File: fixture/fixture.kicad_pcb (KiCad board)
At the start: 2 copper layers, 100 x 100 mm, 40 parts, among them J1 Conn_Coaxial, J10 Conn_Coaxial, J11 Conn_Coaxial, J12 Conn_Coaxial, J13 Conn_Coaxial, J14 Conn_Coaxial, J15 Conn_Coaxial, J16 Conn_Coaxial, J17 Conn_Coaxial, J18 Conn_01x01, J19 Conn_01x01, J2 Conn_Coaxial, J20 Conn_01x01, J21 Conn_01x01, J22 Conn_Coaxial, J23 Conn_Coaxial, J24 Conn_Coaxial, J25 Conn_Coaxial, J26 Conn_01x02, J27 Conn_Coaxial, J28 Conn_01x02, J29 Conn_Coaxial, J3 Conn_Coaxial, J30 Conn_01x01, J31 Conn_01x01, J32 Conn_Coaxial, J4 Conn_02x08_Counter_Clockwise, J5 Conn_02x08_Counter_Clockwise, J6 Conn_Coaxial, J7 Conn_Coaxial, J8 Conn_Coaxial, J9 Conn_Coaxial

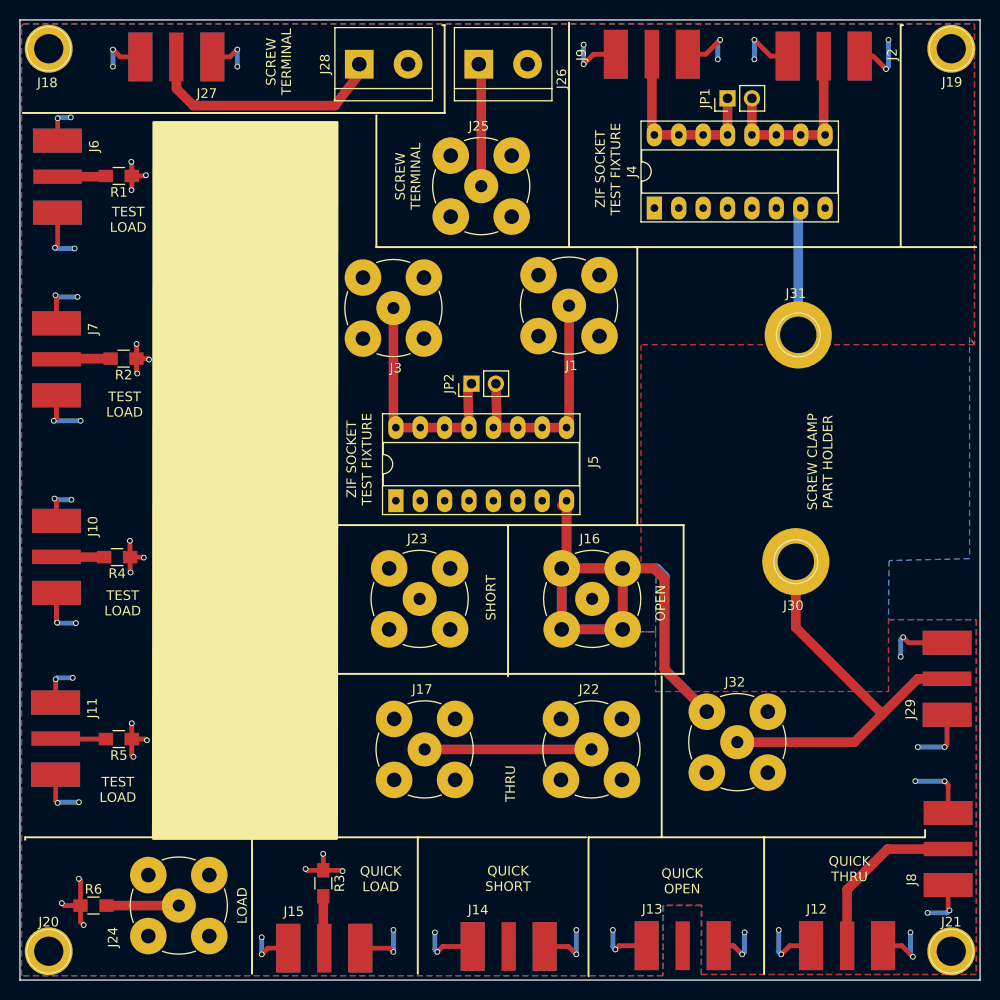
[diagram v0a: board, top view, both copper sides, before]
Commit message: Made more room for handle of ZIF socket
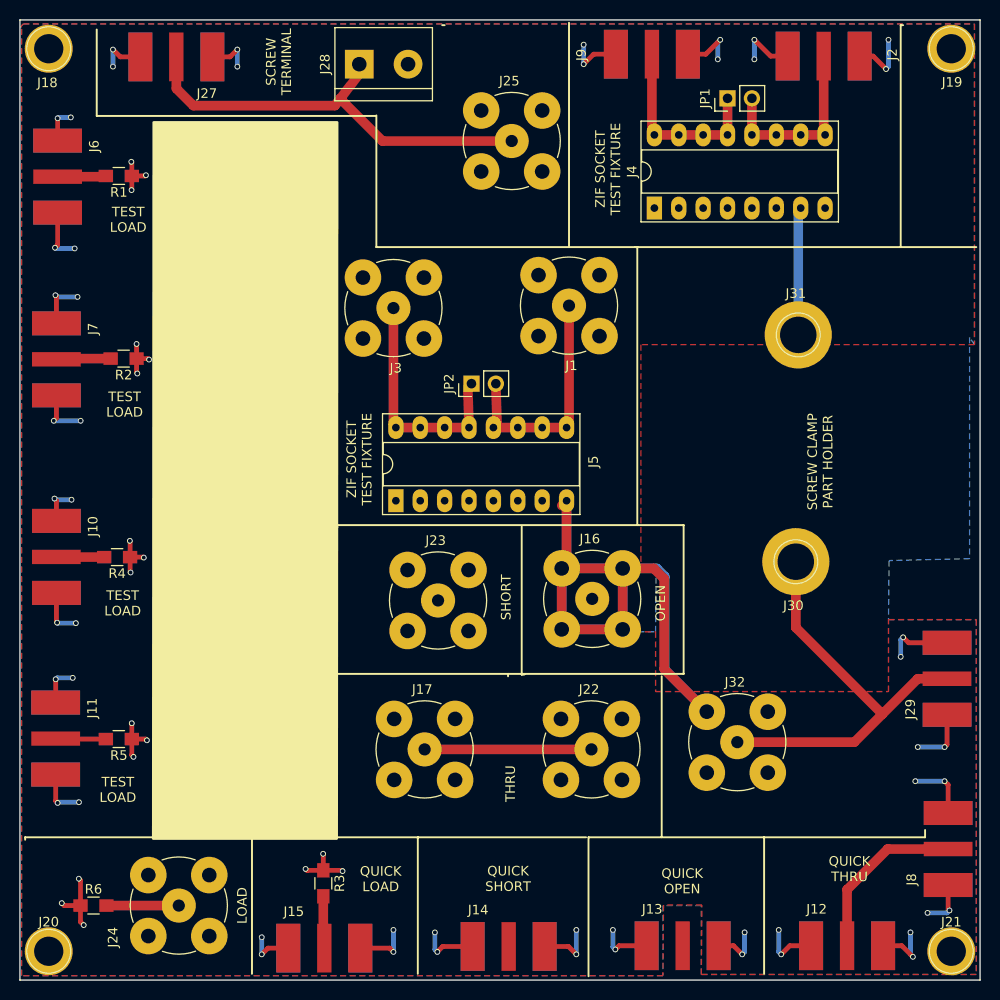
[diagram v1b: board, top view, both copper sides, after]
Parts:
- removed J26: Conn_01x02, Connectors_Terminal_Blocks:TerminalBlock_bornier-2_P5.08mm
- moved J25 5.67 mm to (101.2, 62.6)
- moved J23 1.92 mm to (93.5, 110.5)
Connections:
- J27 pad 1: Net-(J27-Pad1) -> Net-(J25-Pad1)
- J28 pad 1: Net-(J27-Pad1) -> Net-(J25-Pad1)
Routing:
- net Net-(J25-Pad1): track 12.8 -> 45.4 mm
- net Net-(J27-Pad1): track 25.7 -> 0.00 mm
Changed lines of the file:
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@@
 (kicad_pcb (version 4) (host pcbnew 4.0.7)
   (general
-    (links 150)
+    (links 149)
     (no_connects 0)
     (area 49.924999 49.924999 150.075001 150.075001)
     (thickness 1.6)
     (drawings 53)
-    (tracks 283)
+    (tracks 284)
     (zones 0)
-    (modules 40)
-    (nets 17)
+    (modules 39)
+    (nets 16)
   )
   (page A4)
@@
   (net 13 "Net-(J24-Pad1)")
   (net 14 "Net-(J25-Pad1)")
-  (net 15 "Net-(J27-Pad1)")
-  (net 16 "Net-(J29-Pad1)")
+  (net 15 "Net-(J29-Pad1)")
   (net_class Default "This is the default net class."
     (clearance 0.2)
@@
     (add_net "Net-(J24-Pad1)")
     (add_net "Net-(J25-Pad1)")
-    (add_net "Net-(J27-Pad1)")
     (add_net "Net-(J29-Pad1)")
     (add_net "Net-(J3-Pad1)")
@@
   )
   (module Connectors:bnc-ci (layer F.Cu)
-    (at 91.6305 110.2995)
+    (at 93.5482 110.4646)
     (descr "BNC female PCB mount 4 pin straight chassis connector")
     (tags "BNC female PCB mount 4 pin straight chassis connector http://img-asia.electrocomponents.com/largeimages/L457024-02.gif")
@@
   )
   (module Connectors:bnc-ci (layer F.Cu)
-    (at 98.044 67.31)
+    (at 101.219 62.611)
     (descr "BNC female PCB mount 4 pin straight chassis connector")
     (tags "BNC female PCB mount 4 pin straight chassis connector http://img-asia.electrocomponents.com/largeimages/L457024-02.gif")
@@
       (at (xyz 0 0 0))
       (scale (xyz 2 2 2))
-      (rotate (xyz 0 0 0))
-    )
-  )
-  (module Connectors_Terminal_Blocks:TerminalBlock_bornier-2_P5.08mm (layer F.Cu)
-    (at 97.79 54.61)
-    (descr "simple 2-pin terminal block, pitch 5.08mm, revamped version of bornier2")
-    (tags "terminal block bornier2")
-    (fp_text reference J26 (at 8.636 1.524 270) (layer F.SilkS)
-      (effects (font (size 1 1) (thickness 0.15)))
-    )
-    (fp_text value Conn_01x02 (at 2.54 5.08) (layer F.Fab)
-      (effects (font (size 1 1) (thickness 0.15)))
-    )
-    (fp_text user %R (at 2.54 0) (layer F.Fab)
-      (effects (font (size 1 1) (thickness 0.15)))
-    )
-    (fp_line (start -2.41 2.55) (end 7.49 2.55) (layer F.Fab) (width 0.1))
-    (fp_line (start -2.46 -3.75) (end -2.46 3.75) (layer F.Fab) (width 0.1))
-    (fp_line (start -2.46 3.75) (end 7.54 3.75) (layer F.Fab) (width 0.1))
-    (fp_line (start 7.54 3.75) (end 7.54 -3.75) (layer F.Fab) (width 0.1))
-    (fp_line (start 7.54 -3.75) (end -2.46 -3.75) (layer F.Fab) (width 0.1))
-    (fp_line (start 7.62 2.54) (end -2.54 2.54) (layer F.SilkS) (width 0.12))
-    (fp_line (start 7.62 3.81) (end 7.62 -3.81) (layer F.SilkS) (width 0.12))
-    (fp_line (start 7.62 -3.81) (end -2.54 -3.81) (layer F.SilkS) (width 0.12))
-    (fp_line (start -2.54 -3.81) (end -2.54 3.81) (layer F.SilkS) (width 0.12))
-    (fp_line (start -2.54 3.81) (end 7.62 3.81) (layer F.SilkS) (width 0.12))
-    (fp_line (start -2.71 -4) (end 7.79 -4) (layer F.CrtYd) (width 0.05))
-    (fp_line (start -2.71 -4) (end -2.71 4) (layer F.CrtYd) (width 0.05))
-    (fp_line (start 7.79 4) (end 7.79 -4) (layer F.CrtYd) (width 0.05))
-    (fp_line (start 7.79 4) (end -2.71 4) (layer F.CrtYd) (width 0.05))
-    (pad 1 thru_hole rect (at 0 0) (size 3 3) (drill 1.52) (layers *.Cu *.Mask)
-      (net 14 "Net-(J25-Pad1)"))
-    (pad 2 thru_hole circle (at 5.08 0) (size 3 3) (drill 1.52) (layers *.Cu *.Mask)
-      (net 1 GND))
-    (model ${KISYS3DMOD}/Terminal_Blocks.3dshapes/TerminalBlock_bornier-2_P5.08mm.wrl
-      (at (xyz 0.1 0 0))
-      (scale (xyz 1 1 1))
       (rotate (xyz 0 0 0))
     )
@@
       (net 1 GND))
     (pad 1 smd rect (at 0 0 180) (size 1.5 5.08) (layers F.Cu F.Paste F.Mask)
-      (net 15 "Net-(J27-Pad1)"))
+      (net 14 "Net-(J25-Pad1)"))
     (model ${KISYS3DMOD}/Connectors_Amphenol.3dshapes/Amphenol_RF_SMA_132289.wrl
       (at (xyz 0 0 0))
@@
     (fp_line (start 7.79 4) (end -2.71 4) (layer F.CrtYd) (width 0.05))
     (pad 1 thru_hole rect (at 0 0) (size 3 3) (drill 1.52) (layers *.Cu *.Mask)
-      (net 15 "Net-(J27-Pad1)"))
+      (net 14 "Net-(J25-Pad1)"))
     (pad 2 thru_hole circle (at 5.08 0) (size 3 3) (drill 1.52) (layers *.Cu *.Mask)
       (net 1 GND))
@@
       (net 1 GND))
     (pad 1 smd rect (at 0 0 90) (size 1.5 5.08) (layers F.Cu F.Paste F.Mask)
-      (net 16 "Net-(J29-Pad1)"))
+      (net 15 "Net-(J29-Pad1)"))
     (model ${KISYS3DMOD}/Connectors_Amphenol.3dshapes/Amphenol_RF_SMA_132289.wrl
       (at (xyz 0 0 0))
@@
     (fp_circle (center 0 0) (end 0 -2.286) (layer F.SilkS) (width 0.12))
     (pad 1 thru_hole circle (at 0 0) (size 7 7) (drill 3.8) (layers *.Cu *.Mask)
-      (net 16 "Net-(J29-Pad1)"))
+      (net 15 "Net-(J29-Pad1)"))
   )
   (module Connectors:1pin (layer F.Cu)
@@
       (net 1 GND))
     (pad 1 thru_hole circle (at 0 0) (size 3.556 3.556) (drill 1.27) (layers *.Cu *.Mask)
-      (net 16 "Net-(J29-Pad1)"))
+      (net 15 "Net-(J29-Pad1)"))
     (pad 2 thru_hole circle (at 3.175 -3.175) (size 3.81 3.81) (drill 1.524) (layers *.Cu *.Mask)
       (net 1 GND))
@@
     )
   )
+  (gr_line (start 102.2604 118.1862) (end 102.5398 118.1862) (angle 90) (layer F.SilkS) (width 0.2))
+  (gr_line (start 102.2604 102.7684) (end 102.2604 118.1862) (angle 90) (layer F.SilkS) (width 0.2))
+  (gr_line (start 58 60) (end 58 51) (angle 90) (layer F.SilkS) (width 0.2))
+  (gr_line (start 87 60) (end 58 60) (angle 90) (layer F.SilkS) (width 0.2))
   (gr_line (start 141.732 73.66) (end 149.606 73.66) (angle 90) (layer F.SilkS) (width 0.2))
   (gr_line (start 141.732 50.546) (end 141.986 50.546) (angle 90) (layer F.SilkS) (width 0.2))
@@
   (gr_line (start 114.3 102.616) (end 119.126 102.616) (angle 90) (layer F.SilkS) (width 0.2))
   (gr_line (start 100.838 118.11) (end 83.058 118.11) (angle 90) (layer F.SilkS) (width 0.2))
-  (gr_line (start 100.838 102.616) (end 100.838 118.11) (angle 90) (layer F.SilkS) (width 0.2))
   (gr_line (start 83.058 102.616) (end 83.058 102.87) (angle 90) (layer F.SilkS) (width 0.2))
   (gr_line (start 114.3 102.616) (end 83.058 102.616) (angle 90) (layer F.SilkS) (width 0.2))
@@
   (gr_line (start 87.122 59.944) (end 87.122 73.66) (angle 90) (layer F.SilkS) (width 0.2))
   (gr_line (start 94.234 50.546) (end 93.98 50.546) (angle 90) (layer F.SilkS) (width 0.2))
-  (gr_line (start 94.234 59.69) (end 94.234 50.546) (angle 90) (layer F.SilkS) (width 0.2))
-  (gr_line (start 50.292 59.69) (end 94.234 59.69) (angle 90) (layer F.SilkS) (width 0.2))
   (gr_line (start 50.546 135.128) (end 50.546 135.382) (angle 90) (layer F.SilkS) (width 0.2))
   (gr_line (start 74.168 135.128) (end 50.546 135.128) (angle 90) (layer F.SilkS) (width 0.2))
@@
     (effects (font (size 1 1) (thickness 0.15)))
   )
-  (gr_text "SCREW\nTERMINAL\n" (at 90.424 66.294 90) (layer F.SilkS)
-    (effects (font (size 1 1) (thickness 0.15)))
-  )
   (gr_text "SCREW\nTERMINAL\n" (at 76.962 54.356 90) (layer F.SilkS)
     (effects (font (size 1 1) (thickness 0.15)))
@@
     (effects (font (size 1 1) (thickness 0.15)))
   )
-  (gr_text SHORT (at 99.06 110.1725 90) (layer F.SilkS)
+  (gr_text SHORT (at 100.6348 110.1344 90) (layer F.SilkS)
     (effects (font (size 1 1) (thickness 0.15)))
   )
@@
   (segment (start 92.15 125.975) (end 109.525 125.975) (width 1) (layer F.Cu) (net 12) (status 20))
   (segment (start 66.548 142.24) (end 59.008 142.24) (width 1) (layer F.Cu) (net 13))
-  (segment (start 98.044 67.31) (end 98.044 54.864) (width 1) (layer F.Cu) (net 14))
-  (segment (start 98.044 54.864) (end 97.79 54.61) (width 1) (layer F.Cu) (net 14))
-  (segment (start 85.344 54.61) (end 85.344 55.626) (width 1) (layer F.Cu) (net 15) (status 30))
-  (segment (start 85.344 55.626) (end 82.804 58.928) (width 1) (layer F.Cu) (net 15) (status 10))
-  (segment (start 82.804 58.928) (end 68.072 58.928) (width 1) (layer F.Cu) (net 15))
-  (segment (start 68.072 58.928) (end 66.294 57.15) (width 1) (layer F.Cu) (net 15))
-  (segment (start 66.294 57.15) (end 66.294 53.848) (width 1) (layer F.Cu) (net 15))
-  (segment (start 130.81 106.426) (end 130.81 113.284) (width 1) (layer F.Cu) (net 16))
-  (segment (start 130.81 113.284) (end 139.827 122.301) (width 1) (layer F.Cu) (net 16))
-  (segment (start 124.714 125.222) (end 136.906 125.222) (width 1) (layer F.Cu) (net 16))
-  (segment (start 136.906 125.222) (end 139.827 122.301) (width 1) (layer F.Cu) (net 16))
-  (segment (start 139.827 122.301) (end 143.51 118.618) (width 1) (layer F.Cu) (net 16))
-  (segment (start 143.51 118.618) (end 146.558 118.618) (width 1) (layer F.Cu) (net 16))
+  (segment (start 101.219 62.611) (end 87.757 62.611) (width 1) (layer F.Cu) (net 14))
+  (segment (start 87.757 62.611) (end 83.356174 58.210174) (width 1) (layer F.Cu) (net 14))
+  (segment (start 85.344 54.61) (end 85.344 55.626) (width 1) (layer F.Cu) (net 14) (status 30))
+  (segment (start 85.344 55.626) (end 83.356174 58.210174) (width 1) (layer F.Cu) (net 14) (status 10))
+  (segment (start 83.356174 58.210174) (end 82.804 58.928) (width 1) (layer F.Cu) (net 14) (status 10))
+  (segment (start 82.804 58.928) (end 68.072 58.928) (width 1) (layer F.Cu) (net 14))
+  (segment (start 68.072 58.928) (end 66.294 57.15) (width 1) (layer F.Cu) (net 14))
+  (segment (start 66.294 57.15) (end 66.294 53.848) (width 1) (layer F.Cu) (net 14))
+  (segment (start 130.81 106.426) (end 130.81 113.284) (width 1) (layer F.Cu) (net 15))
+  (segment (start 130.81 113.284) (end 139.827 122.301) (width 1) (layer F.Cu) (net 15))
+  (segment (start 124.714 125.222) (end 136.906 125.222) (width 1) (layer F.Cu) (net 15))
+  (segment (start 136.906 125.222) (end 139.827 122.301) (width 1) (layer F.Cu) (net 15))
+  (segment (start 139.827 122.301) (end 143.51 118.618) (width 1) (layer F.Cu) (net 15))
+  (segment (start 143.51 118.618) (end 146.558 118.618) (width 1) (layer F.Cu) (net 15))
   (zone (net 0) (net_name "") (layer F.SilkS) (hatch edge 0.508)
     (connect_pads (clearance 0.5))

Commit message: Changed fixture to use toggle clamp
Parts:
- moved J31 15.3 mm to (145.4, 77.5)
- moved J30 4.06 mm to (130.8, 110.5)
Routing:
- net Net-(J29-Pad1): track 44.2 -> 40.1 mm
- net GND: track 297.3 -> 293.4 mm
- added copper zone on F.Cu, net Net-(J29-Pad1)
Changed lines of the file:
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@@
   )
   (module Connectors:1pin (layer F.Cu)
-    (at 130.81 106.426)
+    (at 130.81 110.49)
     (descr "module 1 pin (ou trou mecanique de percage)")
     (tags DEV)
@@
   )
   (module Connectors:1pin (layer F.Cu)
-    (at 131.064 82.804)
+    (at 145.4 77.5)
     (descr "module 1 pin (ou trou mecanique de percage)")
     (tags DEV)
@@
   (gr_line (start 127.508 135.128) (end 144.272 135.128) (angle 90) (layer F.SilkS) (width 0.2))
   (gr_line (start 127.508 149.352) (end 127.508 135.128) (angle 90) (layer F.SilkS) (width 0.2))
-  (gr_text "SCREW CLAMP\nPART HOLDER" (at 133.35 96.012 90) (layer F.SilkS)
+  (gr_text "SCREW CLAMP\nPART HOLDER" (at 119 93.5 90) (layer F.SilkS)
     (effects (font (size 1 1) (thickness 0.15)))
   )
@@
   (via (at 122.936 52.07) (size 0.6) (drill 0.4) (layers F.Cu B.Cu) (net 1))
   (segment (start 121.436 53.57) (end 122.936 52.07) (width 0.5) (layer F.Cu) (net 1))
-  (segment (start 131.064 82.804) (end 131.064 69.85) (width 1) (layer B.Cu) (net 1))
+  (segment (start 131.318 78.867) (end 131.064 69.85) (width 1) (layer B.Cu) (net 1) (status 10))
   (segment (start 131.064 69.85) (end 131.318 69.596) (width 1) (layer B.Cu) (net 1))
   (segment (start 131.064 69.85) (end 131.318 69.596) (width 1) (layer F.Cu) (net 1))
@@
   (segment (start 68.072 58.928) (end 66.294 57.15) (width 1) (layer F.Cu) (net 14))
   (segment (start 66.294 57.15) (end 66.294 53.848) (width 1) (layer F.Cu) (net 14))
-  (segment (start 130.81 106.426) (end 130.81 113.284) (width 1) (layer F.Cu) (net 15))
+  (segment (start 130.81 110.49) (end 130.81 113.284) (width 1) (layer F.Cu) (net 15) (status 10))
   (segment (start 130.81 113.284) (end 139.827 122.301) (width 1) (layer F.Cu) (net 15))
   (segment (start 124.714 125.222) (end 136.906 125.222) (width 1) (layer F.Cu) (net 15))
@@
     (polygon
       (pts
-        (xy 149.4155 83.82) (xy 148.9075 83.058) (xy 148.9075 106.1085) (xy 140.524762 106.307814) (xy 140.462 112.4585)
+        (xy 149.4155 83.82) (xy 116.1075 83.358) (xy 116.1075 106.4085) (xy 140.524762 106.307814) (xy 140.462 112.4585)
         (xy 149.606 112.4585) (xy 149.606 149.4155) (xy 120.9675 149.4155) (xy 120.9675 142.24) (xy 116.967 142.24)
         (xy 116.967 149.5425) (xy 50.165 149.5425) (xy 50.165 50.7365) (xy 50.038 50.7365) (xy 50.3555 50.419)
@@
       )
     )
+  )
+  (zone (net 15) (net_name "Net-(J29-Pad1)") (layer F.Cu) (hatch edge 0.508)
+    (connect_pads (clearance 0.5))
+    (min_thickness 0.5)
+    (fill yes (arc_segments 16) (thermal_gap 0.508) (thermal_bridge_width 3))
+    (polygon
+      (pts
+        (xy 149.4 84.1) (xy 146.9 84.1) (xy 122 91) (xy 122 106) (xy 126 106)
+        (xy 126 115) (xy 136 115) (xy 136 106) (xy 149 106) (xy 149 85)
+      )
+    )
+  )
+  (zone (net 0) (net_name "") (layer F.Mask) (hatch edge 0.508)
+    (connect_pads (clearance 0.5))
+    (min_thickness 0.5)
+    (fill yes (arc_segments 16) (thermal_gap 0.508) (thermal_bridge_width 3))
+    (polygon
+      (pts
+        (xy 149 74) (xy 121.5 74) (xy 121.5 106.5) (xy 149.5 106.5) (xy 149.5 74)
+      )
+    )
